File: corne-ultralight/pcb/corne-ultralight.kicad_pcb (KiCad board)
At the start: 2 copper layers, 275.5 x 105.6 mm, 132 parts, among them J2 OLED, J5 Breakaway_Tabs, J7 OLED, SW1 SW_PUSH, SW10 SW_PUSH, SW11 SW_PUSH, SW12 SW_PUSH, SW13 SW_PUSH, SW14 SW_PUSH, SW15 SW_PUSH, SW16 SW_PUSH, SW17 SW_PUSH, SW18 SW_PUSH, SW19 SW_PUSH, SW2 SW_PUSH, SW20 SW_PUSH, SW21 SW_PUSH, SW22 SW_PUSH, SW23 SW_PUSH, SW24 SW_PUSH, SW25 SW_PUSH, SW26 SW_PUSH, SW27 SW_PUSH, SW28 SW_PUSH, SW29 SW_PUSH, SW3 SW_PUSH, SW30 SW_PUSH, SW31 SW_PUSH, SW32 SW_PUSH, SW33 SW_PUSH, SW34 SW_PUSH, SW35 SW_PUSH, SW36 SW_PUSH, SW37 SW_PUSH, SW38 SW_PUSH, SW39 SW_PUSH, SW4 SW_PUSH, SW40 SW_PUSH, SW41 SW_PUSH, SW42 SW_PUSH, SW5 SW_PUSH, SW6 SW_PUSH, SW7 SW_PUSH, SW8 SW_PUSH, SW9 SW_PUSH, U1 ProMicro, U2 ProMicro

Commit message: TH Diodes
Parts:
- SW1, SW10, SW11, SW12, SW13, SW14, SW15, SW16, SW17, SW18, SW19, SW2, SW20, SW22, SW23, SW24, SW25, SW26, SW27, SW28, SW29, SW3, SW30, SW31, SW32, SW33, SW34, SW35, SW36, SW37, SW38, SW39, SW4, SW40, SW41, SW5, SW6, SW7, SW8, SW9: footprint gateron-ks27:gateron-ks27-choc-v1-mx -> gateron-ks27:gateron-ks27-choc-v1
- SW21, SW42: footprint gateron-ks27:gateron-ks27-choc-v1-mx-1.5u -> gateron-ks27:gateron-ks27-choc-v1-1.5u
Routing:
- net Net-(D37-Pad2): track 14.2 -> 16.2 mm
- net Net-(BATJ3-Pad2): track 24.7 -> 25.4 mm

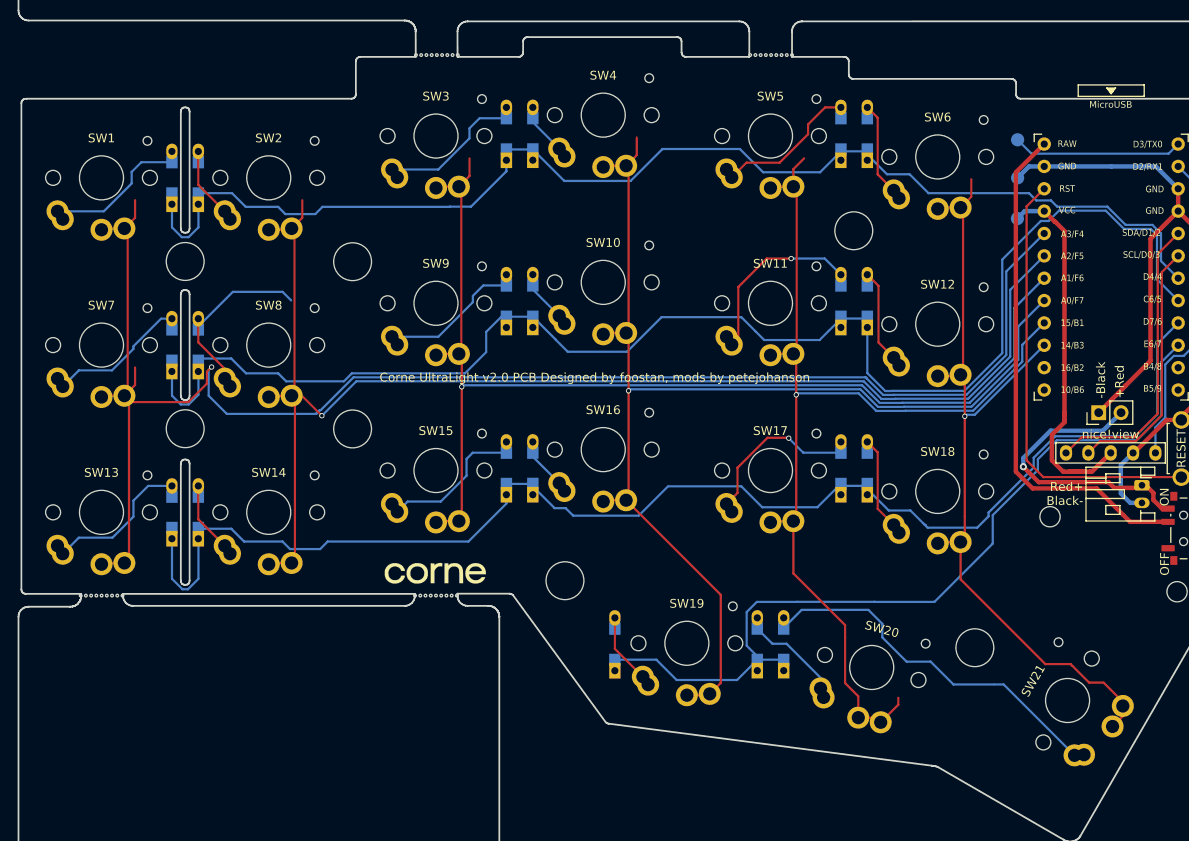
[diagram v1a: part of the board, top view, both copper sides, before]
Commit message: Left side mostly routed
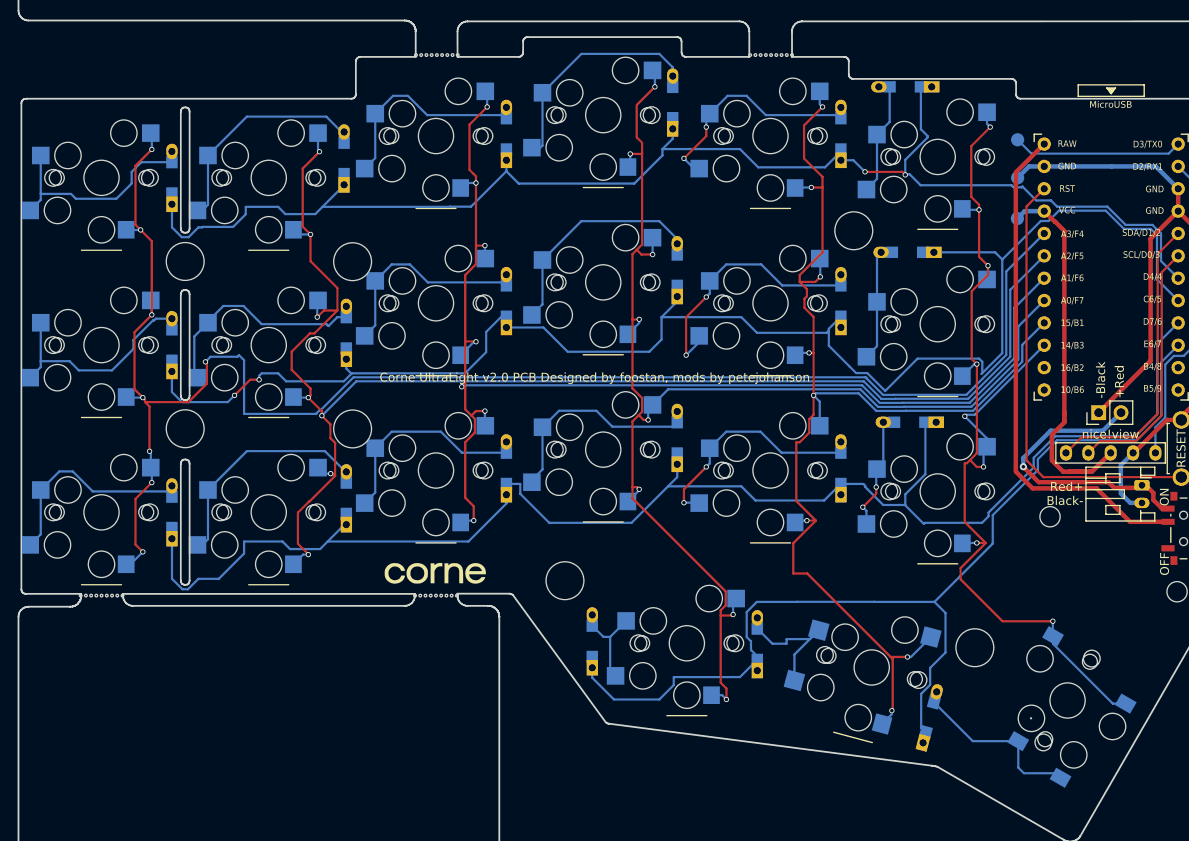
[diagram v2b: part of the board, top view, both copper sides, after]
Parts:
- SW1, SW10, SW11, SW12, SW13, SW14, SW15, SW16, SW17, SW18, SW19, SW2, SW20, SW3, SW4, SW5, SW6, SW7, SW8, SW9: footprint gateron-ks27:gateron-ks27-choc-v1 -> kbd:CherryMX_Choc_Hotswap_BACKONLY
- SW21: footprint gateron-ks27:gateron-ks27-choc-v1-1.5u -> kbd:CherryMX_Choc_Hotswap_1.5u_BACKONLY
- moved D21 18.6 mm to (116.3, 107.2), turned to 75 degrees
- moved D14 16.9 mm to (50.0, 82.3)
- moved D8 16.9 mm to (50.0, 63.5)
- moved D10 16.8 mm to (87.6, 56.4)
- moved D16 16.8 mm to (87.6, 75.5)
- moved D2 16.7 mm to (49.7, 43.7)
- moved D4 16.3 mm to (87.1, 37.4)
- moved D12 7.18 mm to (113.8, 54.4), turned to 180 degrees
- moved D18 7.12 mm to (114.0, 73.7), turned to 180 degrees
- moved D6 6.86 mm to (113.5, 35.6), turned to 180 degrees
- moved D19 2.59 mm to (77.9, 98.6)
- turned SW21 to -30 degrees
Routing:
- net Net-(D21-Pad2): track 42.7 -> 19.7 mm
- net col4: track 116.4 -> 138.9 mm, vias 1 -> 8
- net Net-(D4-Pad2): track 5.92 -> 26.1 mm
- net col5: track 94.4 -> 114.5 mm, vias 1 -> 8
- net Net-(D10-Pad2): track 5.92 -> 25.0 mm
- net col3: track 135.1 -> 153.5 mm, vias 1 -> 8
- net Net-(D16-Pad2): track 5.92 -> 23.5 mm
- net Net-(D14-Pad2): track 9.27 -> 26.2 mm
- net row3: track 98.1 -> 114.6 mm
- net Net-(D2-Pad2): track 9.27 -> 25.6 mm
- net col1: track 150.3 -> 166.0 mm, vias 1 -> 7
- net col2: track 126.5 -> 141.2 mm, vias 1 -> 7
- net row0: track 145.2 -> 156.0 mm, vias 0 -> 2
- net row2: track 158.6 -> 168.1 mm
- net Net-(D7-Pad2): track 17.0 -> 26.3 mm
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
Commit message: Right half changed to hotswaps
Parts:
- SW22, SW23, SW24, SW25, SW26, SW27, SW28, SW29, SW30, SW31, SW32, SW33, SW34, SW35, SW36, SW37, SW38, SW39, SW40, SW41: footprint gateron-ks27:gateron-ks27-choc-v1 -> kbd:CherryMX_Choc_Hotswap_BACKONLY_FLIPPED
- SW42: footprint gateron-ks27:gateron-ks27-choc-v1-1.5u -> kbd:CherryMX_Choc_Hotswap_1.5u_BACKONLY_FLIPPED
- moved D42 19.6 mm to (183.2, 106.7), turned to 105 degrees
- moved D31 16.7 mm to (213.2, 57.6)
- moved D25 16.5 mm to (213.3, 38.5)
- moved D35 16.4 mm to (251.4, 81.7)
- moved D29 16.4 mm to (251.4, 62.8)
- moved D23 16.4 mm to (251.4, 44.1)
- moved D37 16.1 mm to (213.6, 77.9)
- moved D27 6.61 mm to (187.0, 36.2), turned to 0 degrees
- moved D33 6.33 mm to (187.5, 55.1), turned to 0 degrees
- moved D39 5.83 mm to (187.7, 74.7), turned to 0 degrees
- moved D40 2.90 mm to (221.8, 96.5)
- moved D22 0.44 mm to (271.0, 46.3)
- turned SW42 to 30 degrees
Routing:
- net col2_r: track 147.4 -> 193.1 mm, vias 1 -> 7
- net col3_r: track 152.8 -> 183.9 mm, vias 1 -> 9
- net Net-(D42-Pad2): track 41.7 -> 16.8 mm
- net row3_r: track 86.3 -> 106.0 mm, vias 2 -> 3
- net Net-(D22-Pad2): track 9.27 -> 25.3 mm
- net row1_r: track 136.6 -> 152.3 mm, vias 0 -> 2
- net Net-(D34-Pad2): track 9.27 -> 24.7 mm
- net Net-(D28-Pad2): track 9.27 -> 24.7 mm
- net col4_r: track 133.0 -> 148.4 mm, vias 1 -> 9
- net Net-(D36-Pad2): track 9.52 -> 24.7 mm
- net Net-(D24-Pad2): track 9.52 -> 24.7 mm
- net Net-(D30-Pad2): track 9.52 -> 24.6 mm
- net Net-(D38-Pad2): track 9.52 -> 24.6 mm
- net Net-(D32-Pad2): track 9.52 -> 24.6 mm
- net Net-(D26-Pad2): track 9.52 -> 24.6 mm
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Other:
- board text added: "Corne UL v2.1 PCB by foostan/petejohanson, mods by billyjacoby"
- board text added: "rev 1.0"
- board text removed: "Corne Light v2.0 PCB Designed by foostan"
- board text removed: "Corne UltraLight v2.0 PCB Designed by foostan, mods by petejohanson"

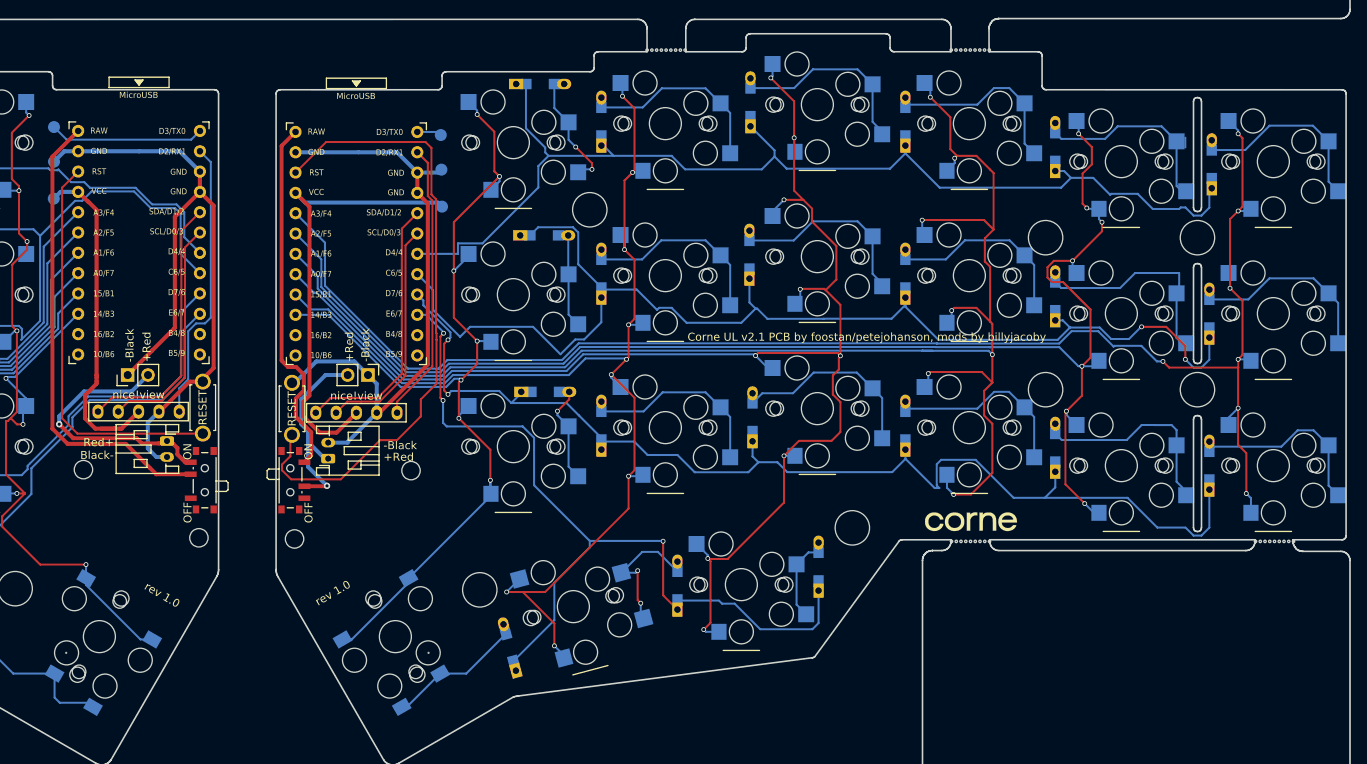
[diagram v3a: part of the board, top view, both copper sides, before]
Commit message: Fixed flipped footprints
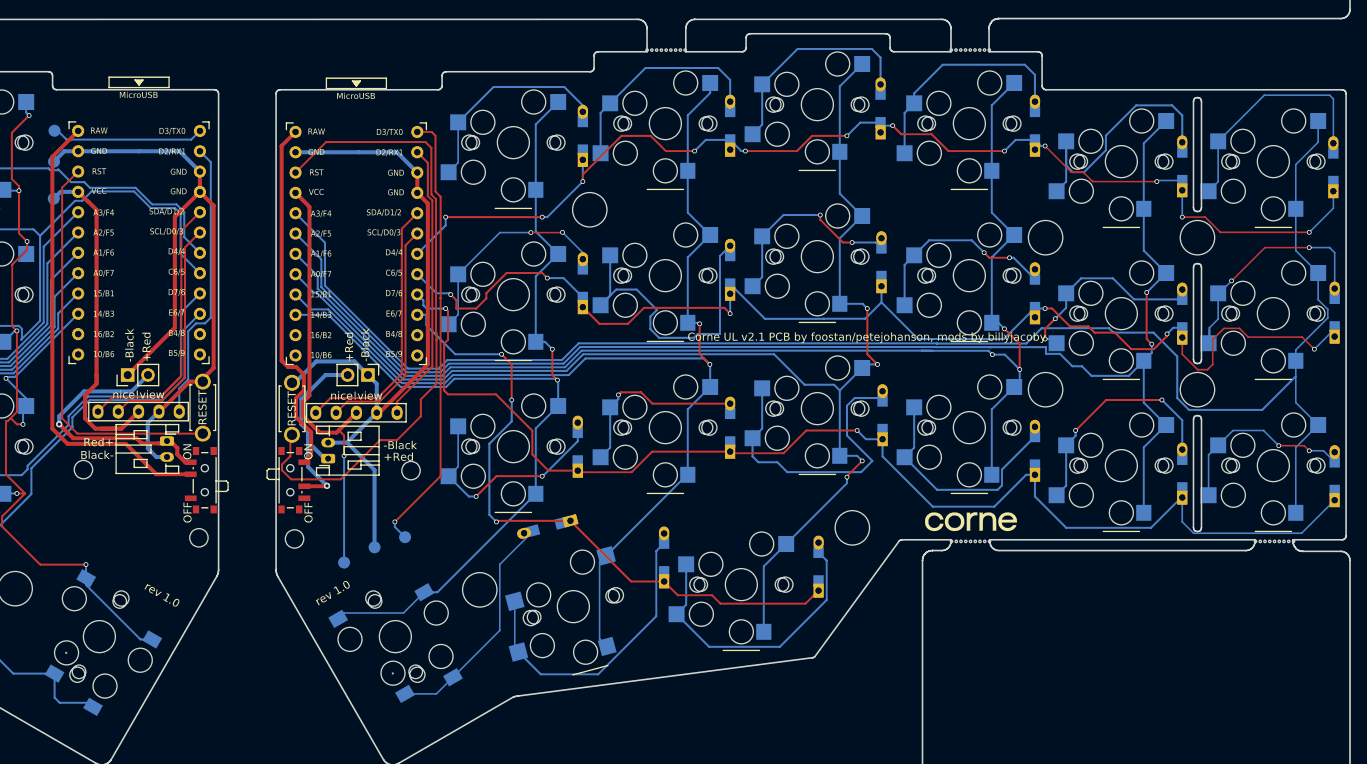
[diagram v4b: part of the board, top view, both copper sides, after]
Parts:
- SW22, SW23, SW24, SW25, SW26, SW27, SW28, SW29, SW30, SW31, SW32, SW33, SW34, SW35, SW36, SW37, SW38, SW39, SW40, SW41: footprint kbd:CherryMX_Choc_Hotswap_BACKONLY_FLIPPED -> kbd:CherryMX_Choc_Hotswap_BACKONLY
- SW42: footprint kbd:CherryMX_Choc_Hotswap_1.5u_BACKONLY_FLIPPED -> kbd:CherryMX_Choc_Hotswap_1.5u_BACKONLY
- moved TP4 50.5 mm to (170.1, 92.9)
- moved TP6 47.9 mm to (166.3, 94.1)
- moved TP5 46.1 mm to (162.5, 96.0)
- moved D31 16.5 mm to (229.7, 58.5)
- moved D36 16.5 mm to (248.9, 82.1)
- moved D30 16.4 mm to (248.9, 62.4)
- moved D25 16.3 mm to (229.6, 39.3)
- moved D37 16.3 mm to (229.8, 77.6)
- moved D24 16.2 mm to (248.9, 41.4)
- moved D35 16.2 mm to (267.3, 84.9)
- moved D26 16.1 mm to (210.8, 41.4)
- moved D32 16.1 mm to (210.8, 59.4)
- moved D38 16.1 mm to (210.8, 79.2)
- moved D23 16.1 mm to (267.3, 46.5)
- moved D29 16.0 mm to (267.3, 64.9)
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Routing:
- net RGB_r: track 3.10 -> 55.8 mm, vias 0 -> 1
- net col2_r: track 193.1 -> 157.2 mm, vias 7 -> 3
- net Net-(D40-Pad2): track 10.1 -> 36.0 mm
- net row3_r: track 106.0 -> 81.6 mm
- net col3_r: track 183.9 -> 165.1 mm, vias 9 -> 4
- net Net-(D41-Pad2): track 18.7 -> 37.4 mm, vias 2 -> 0
- net Net-(D33-Pad2): track 11.6 -> 27.6 mm, vias 0 -> 2
- net Net-(D39-Pad2): track 12.2 -> 27.9 mm, vias 1 -> 2
- net Net-(D37-Pad2): track 24.2 -> 39.3 mm
- net Net-(D32-Pad2): track 24.6 -> 39.3 mm
- net Net-(D27-Pad2): track 14.5 -> 27.1 mm, vias 2 -> 0
- net Net-(D42-Pad2): track 16.8 -> 29.4 mm
- net GNDA: track 76.6 -> 88.0 mm
- net Net-(D23-Pad2): track 24.6 -> 35.5 mm
- net col0_r: track 192.8 -> 203.1 mm, vias 7 -> 0
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
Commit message: removed text, update rev
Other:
- board text added: "rev 2.1"
- board text removed: "Corne UL v2.1 PCB by foostan/petejohanson, mods by billyjacoby"
- board text removed: "rev 1.0"
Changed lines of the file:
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@@
   (gr_line (start 19.677078 94.087041) (end 19.677078 94.087041) (layer "Edge.Cuts") (width 0.2))
   (gr_line (start 167.984992 121.176114) (end 167.857992 121.102454) (layer "Edge.Cuts") (width 0.2))
-  (gr_text "Corne UL v2.1 PCB by foostan/petejohanson, mods by billyjacoby" (at 205.4485 67.841) (layer "F.SilkS")
-    (effects (font (size 1 1) (thickness 0.125)) (justify left))
-  )
-  (gr_text "Corne UL v2.1 PCB by foostan/petejohanson, mods by billyjacoby" (at 53.7675 68.6) (layer "F.SilkS")
-    (effects (font (size 1 1) (thickness 0.125)) (justify left))
-  )
   (gr_text "-Black" (at 167.4375 81.395) (layer "F.SilkS")
     (effects (font (size 1 1) (thickness 0.15)) (justify left))
   )
-  (gr_text "rev 1.0" (at 161.1255 99.845 30) (layer "F.SilkS")
+  (gr_text "rev 2.1" (at 161.1255 99.845 30) (layer "F.SilkS")
     (effects (font (size 1 1) (thickness 0.15)))
   )
@@
     (effects (font (size 1 1) (thickness 0.15)) (justify right))
   )
-  (gr_text "rev 1.0" (at 139.7895 100.099 330) (layer "F.SilkS")
+  (gr_text "rev 2.1" (at 139.7895 100.099 330) (layer "F.SilkS")
     (effects (font (size 1 1) (thickness 0.15)))
   )

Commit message: Added XIAO footprint
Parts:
- removed TP1, TP4: RGB, TestPoint:TestPoint_Pad_D1.5mm
- U1: value ProMicro -> xiao-ble; footprint kbd:ProMicro_v3 -> kleeb-mcu:xiao-ble-tht
- moved U1 6.89 mm to (136.5, 49.7)
- moved TP3 1.93 mm to (124.4, 46.5)
- moved TP2 1.83 mm to (124.4, 50.3)
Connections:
- U1 pad 1: RGB -> row0
- U1 pad 10: row3 -> col2
- U1 pad 11: unconnected-(U1-Pad11) -> col1
- U1 pad 13: unconnected-(U1-Pad13) -> GND
- U1 pad 14: unconnected-(U1-Pad14) -> VCC
- U1 pad 15: col5 -> unconnected-(U1-Pad15)
- U1 pad 16: col4 -> unconnected-(U1-Pad16)
- U1 pad 17: col3 -> reset
- U1 pad 18: col2 -> +5V
- U1 pad 19: col1 -> +BATT
- U1 pad 2: CS -> row1
- U1 pad 20: col0 -> +5V
- U1 pad 21: VCC -> CS
- U1 pad 22: reset -> col5
- U1 pad 3: GND -> row2
- U1 pad 4: GND -> row3
- U1 pad 7: row0 -> col0
- U1 pad 8: row1 -> col4
- U1 pad 9: row2 -> col3
- U2 pad 1: RGB_r -> unconnected-(U2-Pad1)
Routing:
- net RGB_r: track 55.8 -> 0.00 mm, vias 1 -> 0
- net col2_r: track 157.2 -> 193.1 mm, vias 3 -> 7
- net VCC: track 43.1 -> 76.6 mm, vias 0 -> 4
- net row2: track 168.1 -> 198.3 mm
- net row3: track 114.6 -> 144.5 mm
- net Net-(D40-Pad2): track 36.0 -> 10.1 mm
- net row3_r: track 81.6 -> 106.0 mm
- net row0: track 156.0 -> 134.5 mm
- net RGB: track 19.3 -> 0.00 mm
- net col3_r: track 165.1 -> 183.9 mm, vias 4 -> 9
- net Net-(D41-Pad2): track 37.4 -> 18.7 mm, vias 0 -> 2
- net col4: track 138.9 -> 157.5 mm, vias 8 -> 9
- net col3: track 153.5 -> 172.0 mm, vias 8 -> 9
- net col2: track 141.2 -> 159.7 mm, vias 7 -> 8
- net col5: track 114.5 -> 132.7 mm, vias 8 -> 12
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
